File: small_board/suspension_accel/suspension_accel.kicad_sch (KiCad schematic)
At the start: 39 parts, among them IC1 TJA1050T_CM,118, IC2 AMS1117-3.3, IC3 SN74LVC1T45DCKR, IC4 ESP32-S3-MINI-1-N8, IC5 ADS1220IPWR, IC6 TLV75533PDBVR, IC7 SN74LVC1T45DCKR, J1 OSTTE040104, J2 BM04B-GVHS-TB_LF__SN_

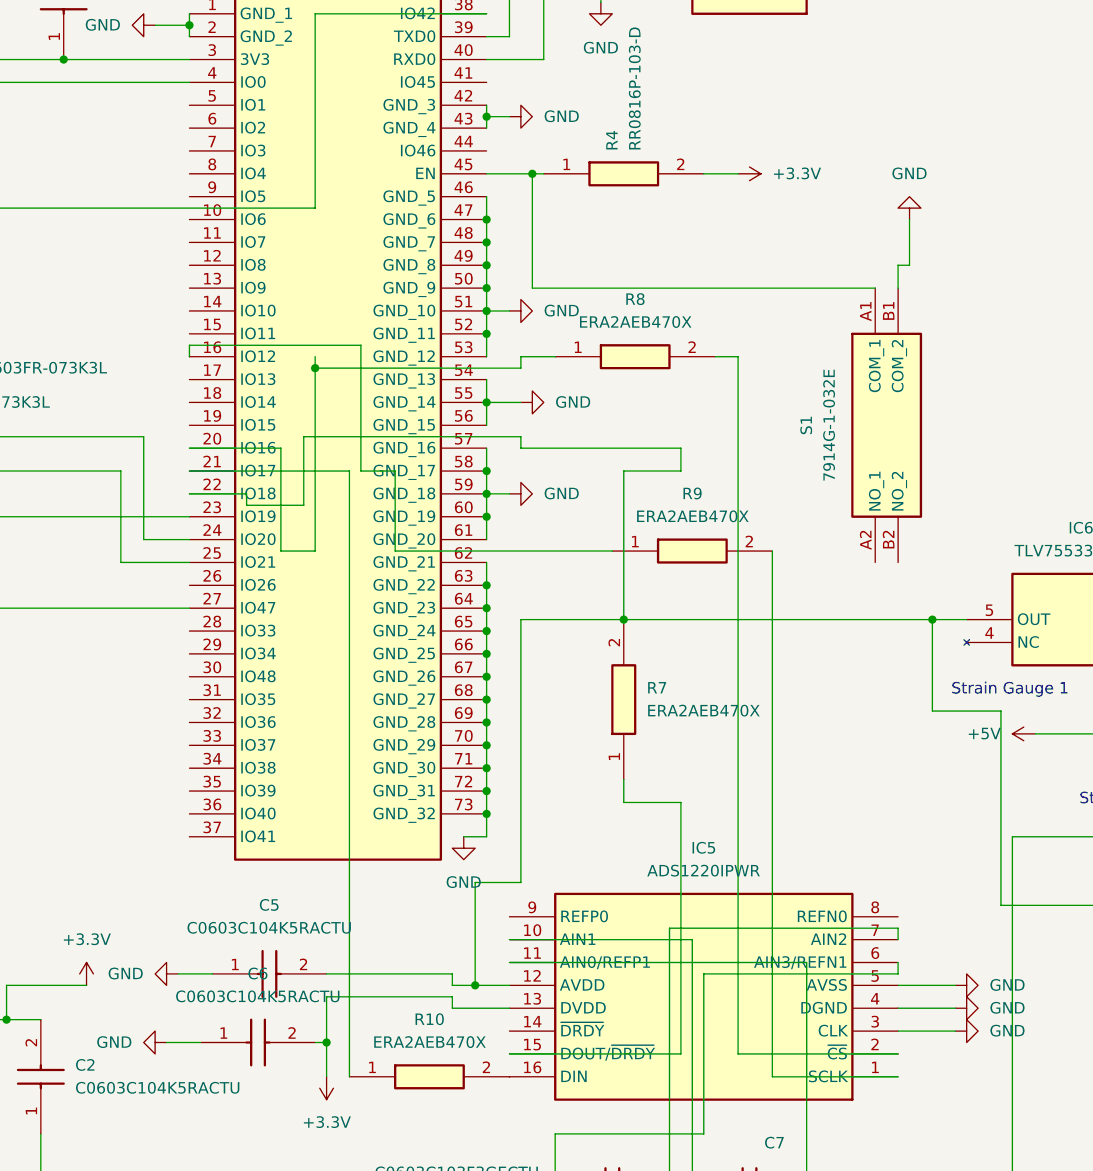
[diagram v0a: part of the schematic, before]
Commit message: finished routing, added logo, widened board for DRC compliance
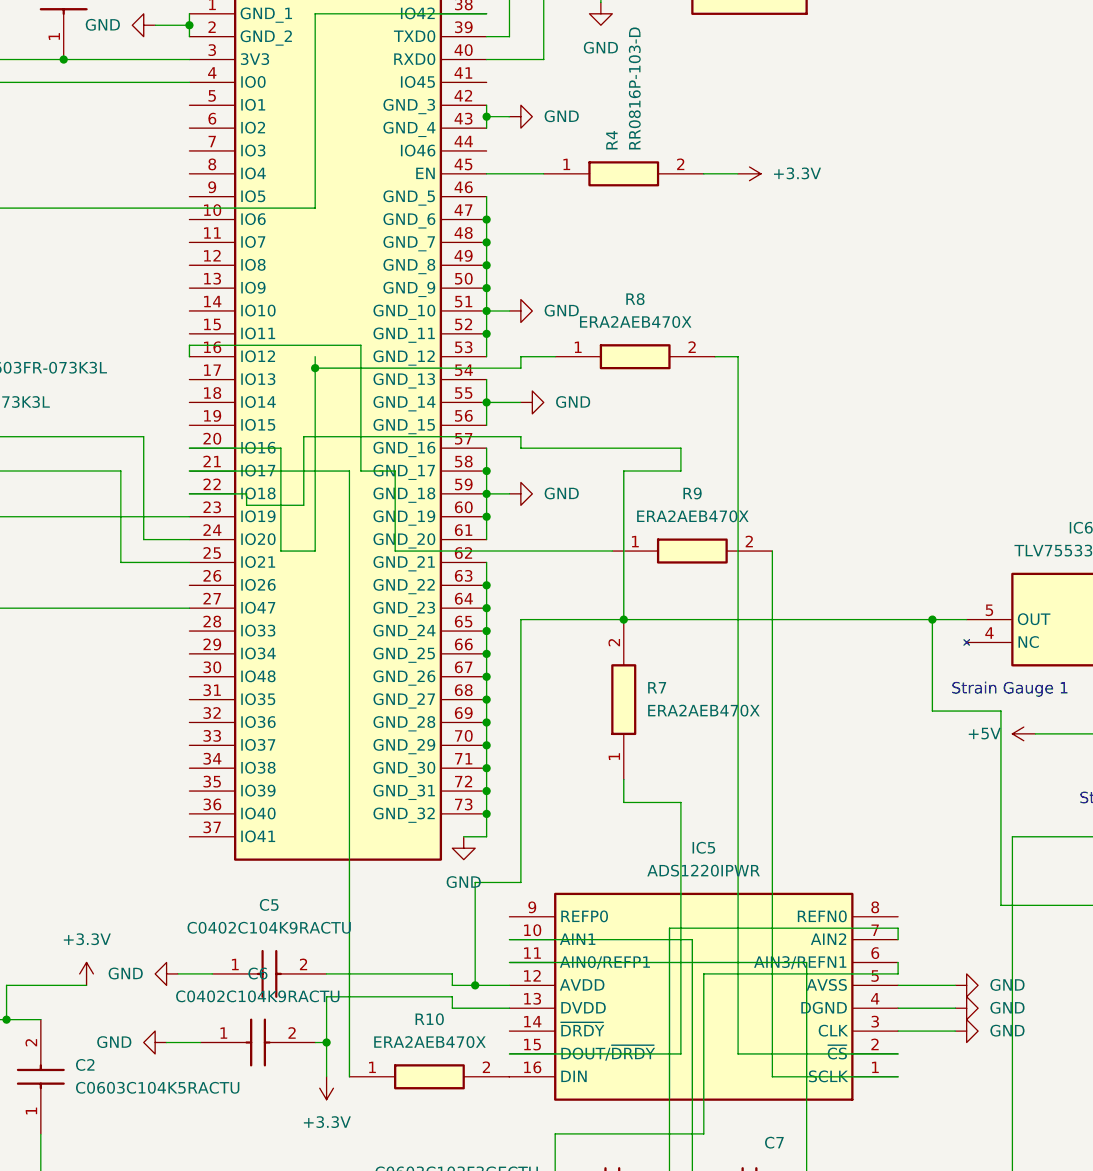
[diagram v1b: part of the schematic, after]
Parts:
- removed C5, C6: C0603C104K5RACTU, C0603, symbol C0603C104K5RACTU:C0603C104K5RACTU
- removed S1: 7914G-1-032E, 7914G1032E, symbol 7914G-1-032E:7914G-1-032E
- added C5, C6: C0402C104K9RACTU, C0402C104J4RACTU, symbol C0402C104K9RACTU:C0402C104K9RACTU
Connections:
- net +3.3V: now also C6.2
- net GND: now also C5.1, C6.1
- net at IC4.22 (IO18), IC5.12 (AVDD), IC6.5 (OUT)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: now also C5.2

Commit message: added supply line TVS
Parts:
- added D5: D5V0F1U2LP-7B, D5V0F1U2LP7B, symbol D5V0F1U2LP-7B:D5V0F1U2LP-7B
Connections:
- net GND: now also D5.2 (A)
- net at J1.1, J2.4, MOS1.3 (D): now also D5.1 (K)

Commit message: spaced out routing a bit
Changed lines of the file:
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@@
-	)
-	(junction
-		(at 92.71 13.97)
-		(diameter 0)
-		(color 0 0 0 0)
 	)
 	(junction
@@
 	)
 	(junction
+		(at 99.06 13.97)
+		(diameter 0)
+		(color 0 0 0 0)
+	)
+	(junction
 		(at 184.15 76.2)
 		(diameter 0)
@@
 	(wire
 		(pts
-			(xy 92.71 13.97) (xy 196.85 13.97)
-		)
-		(stroke
-			(width 0)
-			(type default)
-		)
-	)
-	(wire
-		(pts
 			(xy 182.88 139.7) (xy 182.88 151.13)
 		)
@@
 	(wire
 		(pts
-			(xy 20.32 -8.89) (xy 20.32 38.1)
+			(xy 26.67 6.35) (xy 26.67 38.1)
 		)
 		(stroke
@@
 	(wire
 		(pts
+			(xy 99.06 13.97) (xy 196.85 13.97)
+		)
+		(stroke
+			(width 0)
+			(type default)
+		)
+	)
+	(wire
+		(pts
 			(xy 228.6 214.63) (xy 231.14 214.63)
 		)
@@
 	(wire
 		(pts
-			(xy 20.32 38.1) (xy 33.02 38.1)
+			(xy 26.67 38.1) (xy 33.02 38.1)
 		)
 		(stroke
@@
 	(wire
 		(pts
+			(xy 99.06 13.97) (xy 92.71 13.97)
+		)
+		(stroke
+			(width 0)
+			(type default)
+		)
+	)
+	(wire
+		(pts
 			(xy 143.51 93.98) (xy 143.51 104.14)
 		)
@@
 	(wire
 		(pts
-			(xy 92.71 13.97) (xy 92.71 -8.89)
+			(xy 99.06 13.97) (xy 99.06 6.35)
 		)
 		(stroke
@@
 	(wire
 		(pts
-			(xy 20.32 -8.89) (xy 92.71 -8.89)
-		)
-		(stroke
+			(xy 26.67 6.35) (xy 99.06 6.35)
+		)
+		(stroke
